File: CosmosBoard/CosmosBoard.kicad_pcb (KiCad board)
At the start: 2 copper layers, 200 x 100 mm, 124 parts, among them J1 VIN, J10 Conn_01x04, J11 Conn_01x06, J12 Conn_01x25, J13 Conn_01x08, J14 Conn_01x07, J15 Conn_01x05, J16 Conn_01x04, J17 Conn_01x03, J18 Conn_01x03, J19 Conn_01x04, J2 USB_B_Micro, J20 Conn_01x02, J3 power_jumper, J4 Conn_01x25, J5 Conn_01x02, J6 Conn_01x02, J7 Conn_01x02, J8 Conn_01x02, J9 Conn_01x08, M1 Motor_Servo, M2 Motor_Servo, M3 Motor_Servo, M4 Motor_Servo, P1 SWD, SW1 SW_SPDT, SW10 SW_Push_SPDT, SW11 SW_Push_SPDT, SW2 SW_Push, SW3 SW_Push, SW4 SW_Push, SW5 SW_Push, SW6 SW_Push, SW7 RotaryEncoder_Switch, SW8 SW_Push_SPDT, SW9 SW_Push_SPDT, U1 STM32F405RGT6, U2 BNO055, U3 AMS1117-3.3, U4 BMP280, U5 E32-915T30S, U6 AMS1117-3.3, U7 AMS1117-3.3, X1 8MHz 10ppm (X50328MSB2GI), Y1 32.768, Y2 32.768

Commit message: alligns
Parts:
- J11: value Conn_01x06 -> Conn_01x05; footprint Connector_PinHeader_2.54mm:PinHeader_1x06_P2.54mm_Vertical -> Connector_PinHeader_2.54mm:PinHeader_1x05_P2.54mm_Vertical
- moved C17 305.0 mm to (83.8, 51.5)
- moved C18 305.0 mm to (95.0, 48.5)
- moved D2 305.0 mm to (80.8, 44.2)
- moved J2 305.0 mm to (93.6, 39.1)
- moved J3 305.0 mm to (97.8, 48.6)
- moved R6 305.0 mm to (80.8, 47.8)
- moved U3 305.0 mm to (89.5, 52.1)
- moved J1 304.8 mm to (105.2, 39.5)
- moved J6 296.8 mm to (179.1, 103.7), turned to 180 degrees
- moved R9 290.0 mm to (182.1, 102.1), turned to 90 degrees
- moved J19 287.8 mm to (133.5, 126.7), turned to 90 degrees
- moved J5 286.0 mm to (185.1, 103.7), turned to 180 degrees
- moved J20 285.3 mm to (150.2, 114.8)
- moved R7 279.3 mm to (188.1, 102.1), turned to 90 degrees
- moved J9 276.7 mm to (182.9, 86.9), turned to 90 degrees
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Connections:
- J11 pad 1: /SENSORS/AUX -> Net-(J11-Pin_1)
- J11 pad 5: Net-(J11-Pin_5) -> /SENSORS/AUX
- U5 pad 1: Net-(J11-Pin_5) -> Net-(J11-Pin_1)
- U5 pad 18: /SENSORS/ANT -> unconnected-(U5-ANT-Pad18)
- U5 pad 2: Net-(J11-Pin_4) -> Net-(J11-Pin_2)
- U5 pad 4: Net-(J11-Pin_2) -> Net-(J11-Pin_4)

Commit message: traces
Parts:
- removed J1: VIN, Connector_JST:JST_GH_SM02B-GHS-TB_1x02-1MP_P1.25mm_Horizontal
- added J21: Barrel_Jack_Switch, Connector_BarrelJack:BarrelJack_GCT_DCJ200-10-A_Horizontal, F.Cu at (107.7, 46.9)
- SW2: footprint Button_Switch_THT:SW_PUSH-12mm -> Button_Switch_SMD:SW_Push_SPST_NO_Alps_SKRK
- moved C36 148.5 mm to (91.8, 71.6), turned to 0 degrees
- moved U7 147.3 mm to (89.4, 76.4), turned to 180 degrees
- moved C37 142.6 mm to (95.4, 77.8), turned to 90 degrees
- moved SW9 136.1 mm to (102.0, 76.6), turned to 90 degrees
- moved R27 134.3 mm to (98.0, 69.1)
- moved D11 134.3 mm to (96.3, 69.3)
- moved U6 106.6 mm to (89.2, 63.1), turned to 180 degrees
- moved C35 104.9 mm to (91.4, 58.2)
- moved C34 103.1 mm to (95.2, 64.2), turned to 90 degrees
- moved D10 89.6 mm to (96.2, 57.6), turned to 90 degrees
- moved SW8 88.6 mm to (102.1, 62.2), turned to -90 degrees
- moved R26 87.6 mm to (98.2, 57.6), turned to -90 degrees
- moved SW2 53.3 mm to (125.0, 48.4), turned to -90 degrees
- moved C5 31.0 mm to (117.2, 51.4), turned to 90 degrees
- moved C17 22.5 mm to (105.8, 55.8), turned to 90 degrees
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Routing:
- net +3V3: track 0.00 -> 695.7 mm, vias 0 -> 20
- net +5V: track 0.00 -> 201.6 mm, vias 0 -> 1
- net Net-(U5-VCC): track 0.00 -> 180.6 mm
- net GND: track 0.00 -> 172.1 mm, vias 0 -> 52
- net Net-(J14-Pin_2): track 0.00 -> 167.9 mm
- net USB_D+: track 0.00 -> 58.7 mm
- net USB_D-: track 0.00 -> 58.4 mm
- net Net-(J17-Pin_3): track 0.00 -> 54.0 mm
- net /SENSORS/BTN_4: track 0.00 -> 49.6 mm
- net /SENSORS/SCL_disp: track 0.00 -> 47.6 mm
- net /SENSORS/SDA_disp: track 0.00 -> 47.5 mm
- net /SENSORS/DC_disp: track 0.00 -> 47.5 mm
- net /SENSORS/BLK_disp: track 0.00 -> 47.5 mm
- net /SENSORS/RES_disp: track 0.00 -> 47.5 mm
- net PA4: track 0.00 -> 43.3 mm, vias 0 -> 1
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- added copper zone on In1.Cu, net GND
- added copper zone on In2.Cu, net GND
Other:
- copper layers 2 -> 4

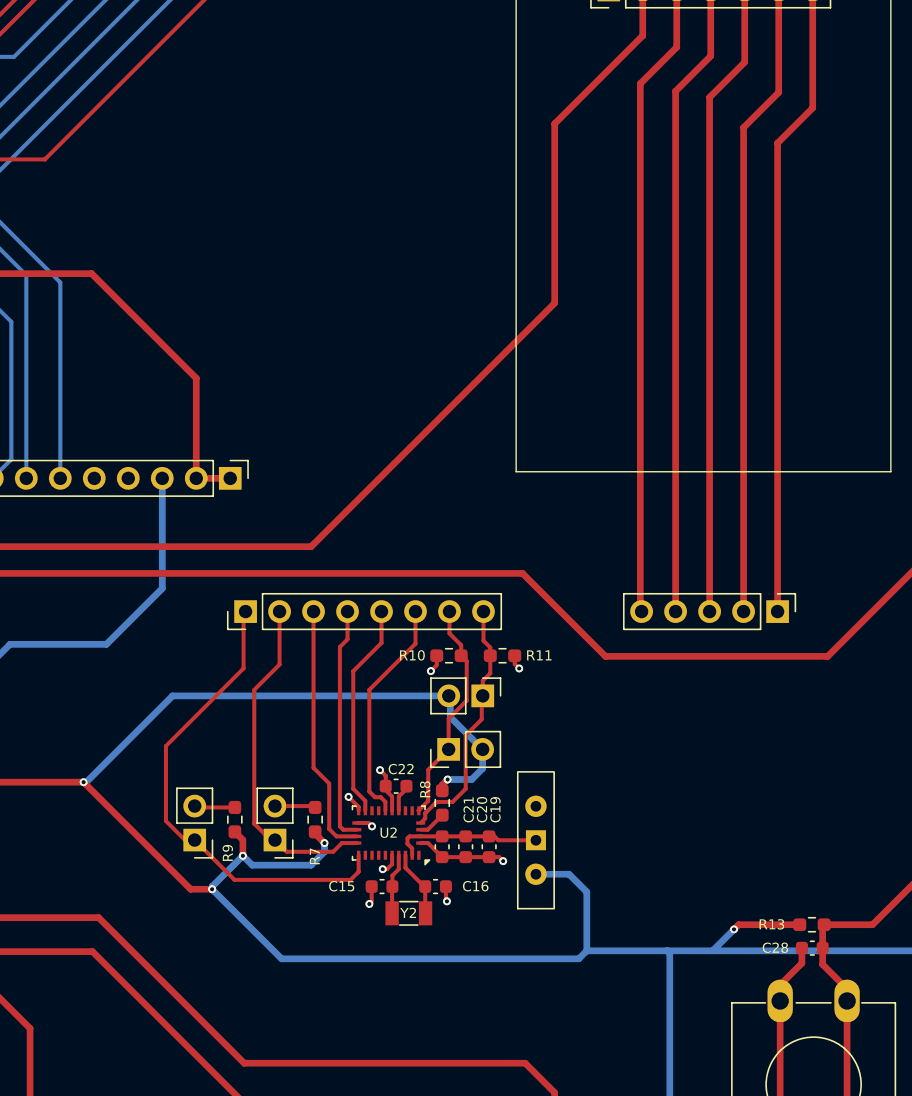
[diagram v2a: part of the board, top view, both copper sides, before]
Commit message: box for bno
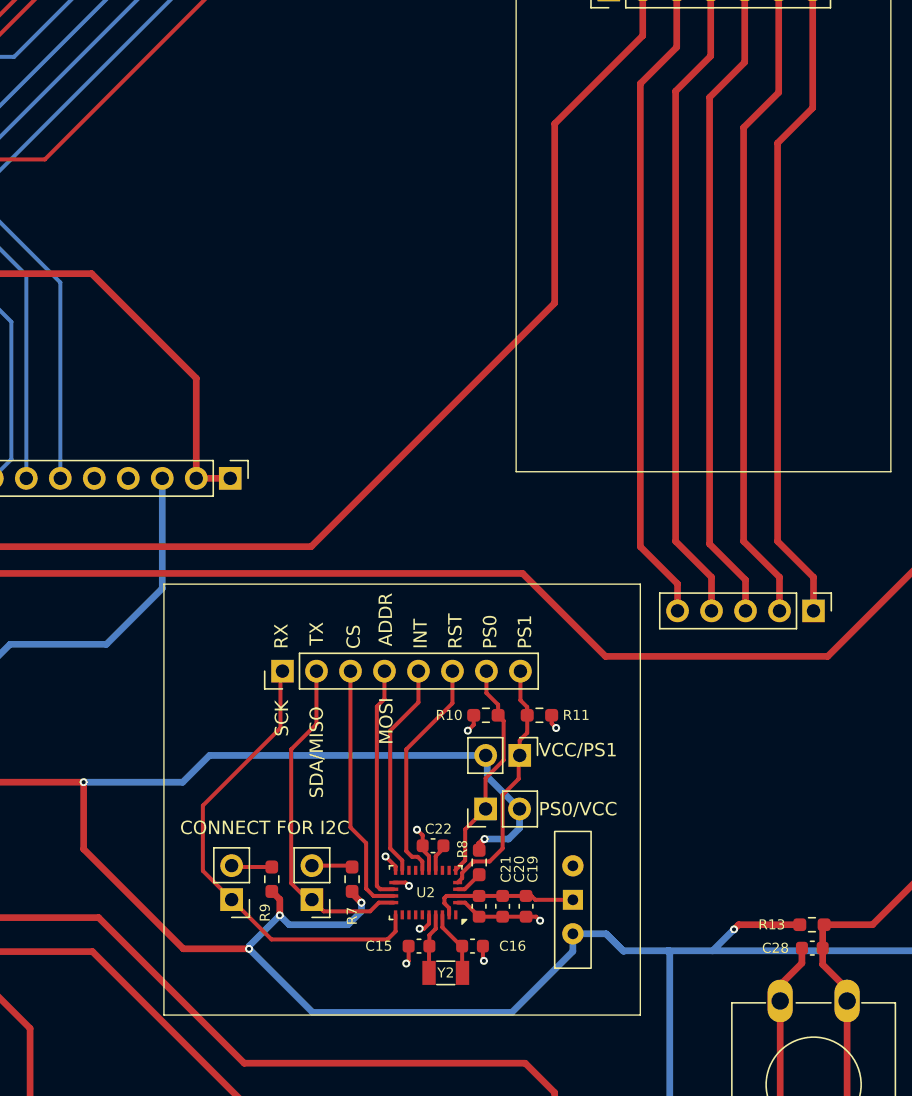
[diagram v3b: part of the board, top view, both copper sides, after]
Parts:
- moved C22 5.24 mm to (193.9, 106.8)
- moved C15 5.24 mm to (192.9, 114.2)
- moved C16 5.24 mm to (196.9, 114.2)
- moved C19 5.24 mm to (200.9, 111.3)
- moved C20 5.24 mm to (199.1, 111.3)
- moved J5 5.24 mm to (184.9, 110.8)
- moved J6 5.24 mm to (178.9, 110.8)
- moved J7 5.24 mm to (197.8, 104.0)
- moved R10 5.24 mm to (197.9, 97.0)
- moved R11 5.24 mm to (201.9, 97.0)
- moved SW10 5.24 mm to (204.4, 110.8)
- moved U2 5.24 mm to (193.4, 110.2)
- moved R9 5.24 mm to (181.9, 109.3)
- moved C21 5.24 mm to (197.3, 111.3)
- moved J8 5.24 mm to (200.4, 100.0)
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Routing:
- net +3V3: track 695.7 -> 698.0 mm
- net /SENSORS/SCL_disp: track 47.6 -> 48.7 mm
- net /SENSORS/SDA_disp: track 47.5 -> 48.6 mm
- net /SENSORS/RES_disp: track 47.5 -> 48.6 mm
- net /SENSORS/DC_disp: track 47.5 -> 48.6 mm
- net /SENSORS/BLK_disp: track 47.5 -> 48.6 mm
- net /SENSORS/SPI_2_MISO_I2C_SDA_UART_TX: track 35.5 -> 34.9 mm
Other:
- board text added: "ADDR"
- board text added: "CONNECT FOR I2C"
- board text added: "CS"
- board text added: "INT"
- board text added: "MOSI"
- board text added: "PS0"
- board text added: "PS0/VCC"
- board text added: "PS1"
- board text added: "RST"
- board text added: "RX"
- board text added: "SDA/MISO"
- board text added: "TX"
- board text added: "VCC/PS1"

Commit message: pre-final
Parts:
- RV1, RV2, RV3: footprint Potentiometer_THT:Potentiometer_Omeg_PC16BU_Vertical -> Potentiometer_THT:Potentiometer_TT_P0915N
- moved C15 53.8 mm to (143.3, 135.0)
- moved C16 53.8 mm to (147.3, 135.0)
- moved C19 53.8 mm to (151.3, 132.0)
- moved C20 53.8 mm to (149.5, 132.0)
- moved C21 53.8 mm to (147.8, 132.0)
- moved C22 53.8 mm to (144.3, 127.5)
- moved J5 53.8 mm to (135.3, 131.5)
- moved J6 53.8 mm to (129.3, 131.5)
- moved J7 53.8 mm to (148.2, 124.8)
- moved J9 53.8 mm to (133.1, 114.4)
- moved R10 53.8 mm to (148.3, 117.8)
- moved R11 53.8 mm to (152.3, 117.8)
- moved R7 53.8 mm to (138.3, 130.0)
- moved R8 53.8 mm to (147.8, 128.7)
- moved R9 53.8 mm to (132.3, 130.0)
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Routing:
- net Net-(J17-Pin_3): track 54.0 -> 14.7 mm
- net +3V3: track 698.0 -> 668.6 mm, vias 20 -> 19
- net Net-(J17-Pin_1): track 15.5 -> 44.6 mm
- net Net-(J19-Pin_4): track 10.5 -> 36.9 mm
- net +5V: track 201.6 -> 226.0 mm
- net Net-(J19-Pin_3): track 19.4 -> 38.9 mm
- net Net-(J19-Pin_2): track 23.1 -> 38.9 mm
- net USB_D-: track 58.4 -> 68.2 mm
- net USB_D+: track 58.7 -> 68.5 mm
- net /SENSORS/SCL_disp: track 48.7 -> 39.4 mm
- net /SENSORS/RES_disp: track 48.6 -> 39.3 mm
- net /SENSORS/DC_disp: track 48.6 -> 39.3 mm
- net /SENSORS/SDA_disp: track 48.6 -> 39.3 mm
- net /SENSORS/BLK_disp: track 48.6 -> 39.3 mm
- net Net-(J11-Pin_4): track 23.8 -> 16.8 mm
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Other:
- board size 200 x 100 mm -> 203.2 x 100 mm
- board text added: "+3.3V"
- board text added: "+5V"
- board text added: "3 2 1"
- board text added: "A"
- board text added: "ADC"
- board text added: "AUX"
- board text added: "B"
- board text added: "BLK"
- board text added: "BMP280"
- board text added: "BTN_1"
- board text added: "BTN_2"
- board text added: "BTN_3"
- board text added: "BTN_4"
- board text added: "BUTTONS"
- board text added: "DC"
- board text added: "ENCODER"
- board text added: "GND"
- board text added: "GPS"
- board text added: "IMU"
- board text added: "LCD"
- board text added: "LED_1"
- board text added: "LED_2"
- board text added: "LED_3"
- board text added: "LED_4"
- board text added: "LORAWAN"
- board text added: "M0"
- board text added: "M1"
- board text added: "PA0"
- board text added: "PA1"
- board text added: "PA10"
- board text added: "PA15"
- board text added: "PA2"
- board text added: "PA3"
- board text added: "PA4"
- board text added: "PA5"
- board text added: "PA6"
- board text added: "PA7"
- board text added: "PA8"
- board text added: "PA9"
- board text added: "PB0"
- board text added: "PB1"
- board text added: "PB10"
- board text added: "PB11"
- board text added: "PB12"
- board text added: "PB13"
- board text added: "PB14"
- board text added: "PB15"
- board text added: "PB2"
- board text added: "PB3"
- board text added: "PB4"
- board text added: "PB5"
- board text added: "PB6"
- board text added: "PB7"
- board text added: "PB8"
- board text added: "PB9"
- board text added: "PC0"
- board text added: "PC1"
- board text added: "PC10"
- board text added: "PC11"
- board text added: "PC12"
- board text added: "PC13"
- board text added: "PC2"
- board text added: "PC3"
- board text added: "PC4"
- board text added: "PC5"
- board text added: "PC6"
- board text added: "PC7"
- board text added: "PC8"
- board text added: "PC9"
- board text added: "PD2"
- board text added: "POWER"
- board text added: "RES"
- board text added: "SCL"
- board text added: "SDA"
- board text added: "STM32F405"
- board text added: "SW"
- board text added: "Servo"
